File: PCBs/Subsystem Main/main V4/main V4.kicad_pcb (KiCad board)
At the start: 4 copper layers, 134.4 x 128.8 mm, 33 parts, among them J1 DCJ0303, SW1 L02P, SW2 L02P, SW3 L02P, SW4 L02P, SW5 L02P, SW6 L02P, SW7 L02P, SW8 L02P, X1 W237-103

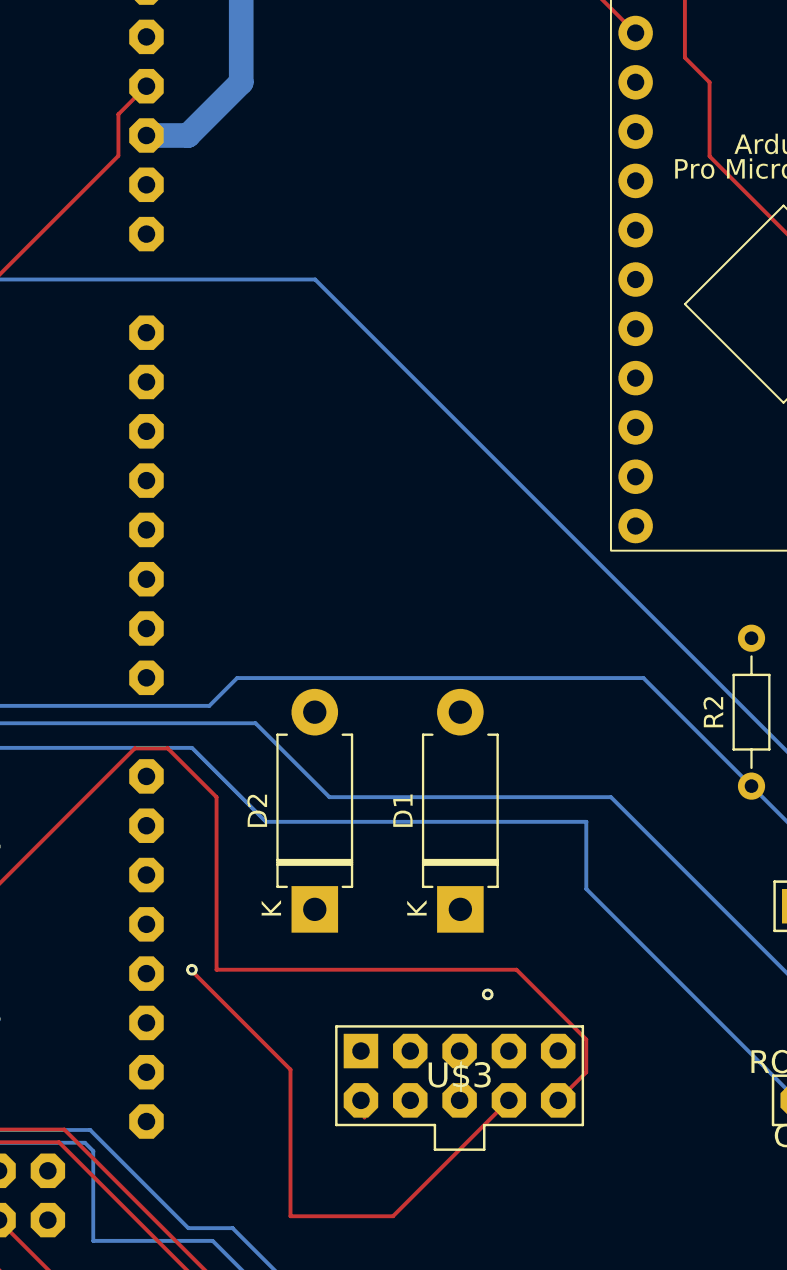
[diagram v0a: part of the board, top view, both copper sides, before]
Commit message: Fixed the headers to include reset for the SPI interface and expansion for future touch control if wanted
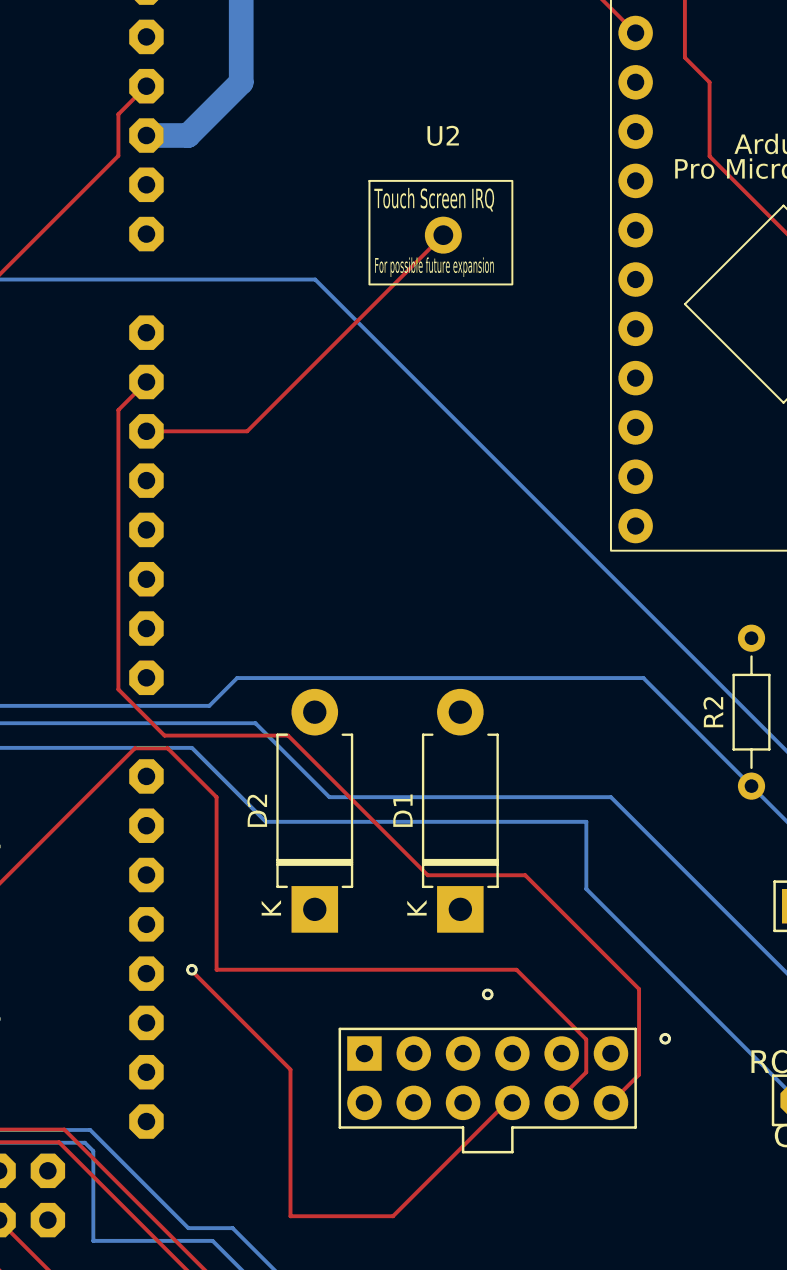
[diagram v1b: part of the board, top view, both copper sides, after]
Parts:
- removed U$3: SPI_HEADERSPI_HEADER_RIBBON_CONNECTOR, main:SPI_HEADER_RIBBON_CONNECTOR
- added C1: ~, Subsystem Main Extra Symbols:SPI_HEADER_RIBBON_CONNECTOR_V2, F.Cu at (168.9, 133.9)
- added U2: ~, Subsystem Main Extra Symbols:T_IRQ, F.Cu at (166.6, 90.4)
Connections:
- U$1 pad A1: unconnected-(U$1-PadA1) -> /Touch_CS
- U$1 pad A2: unconnected-(U$1-PadA2) -> Net-(U2-T_IRQ)
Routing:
- net /RESET: track 156.4 -> 215.9 mm
- net /Touch_CS: track 0.00 -> 56.1 mm
- net Net-(U2-T_IRQ): track 0.00 -> 19.5 mm
- net /MOSI: track 49.2 -> 56.1 mm, vias 1 -> 2

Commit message: various fabrication outputs
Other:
- board text added: "Subsytem Main Board CMSC V4.0 10/2/24 Nathan Ford"
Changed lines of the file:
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@@
 		(layer "Edge.Cuts")
+	)
+	(gr_text "Subsytem Main Board\nCMSC\nV4.0 10/2/24\nNathan Ford"
+		(at 69.342 100.076 -90)
+		(layer "F.SilkS")
+		(effects
+			(font
+				(size 1.5 1.5)
+				(thickness 0.3)
+				(bold yes)
+			)
+			(justify bottom)
+		)
 	)
 	(via

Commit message: added neopixel stabalization
added capacitor slot and resistor slot, both are optional but can be added to increase stability.
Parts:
- removed 1: ~, main:ETHERNET_ADAPTER
- added 11: ~, main:ETHERNET_ADAPTER, F.Cu at (162.4, 48.1)
- added C2: C_Polarized, Capacitor_THT:CP_Radial_D10.0mm_P2.50mm_P5.00mm, F.Cu at (81.4, 133.3)
- added Neopixel Resistor: 350 ohm, Resistor_THT:R_Axial_DIN0204_L3.6mm_D1.6mm_P7.62mm_Horizontal, F.Cu at (95.5, 120.1)
- R1: value FLIPFLOP-RES -> 220 ohm
- R2: value FLIPFLOP-RES -> 10K
- R3: value FLIPFLOP-RES -> 10k
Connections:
- U$1 pad D8: Net-(X1B-KL) -> Net-(Neopixel Resistor1-Pad1)
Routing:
- net Net-(X1B-KL): track 82.3 -> 37.7 mm
- net Net-(Neopixel Resistor1-Pad1): track 0.00 -> 38.2 mm
- net /5V: track 330.7 -> 341.1 mm
- net GND: track 491.5 -> 501.7 mm
